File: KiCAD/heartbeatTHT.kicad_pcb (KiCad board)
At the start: 2 copper layers, 48.7 x 39.3 mm, 17 parts, among them Q1 BC547, Q2 BC547, Q3 BC557

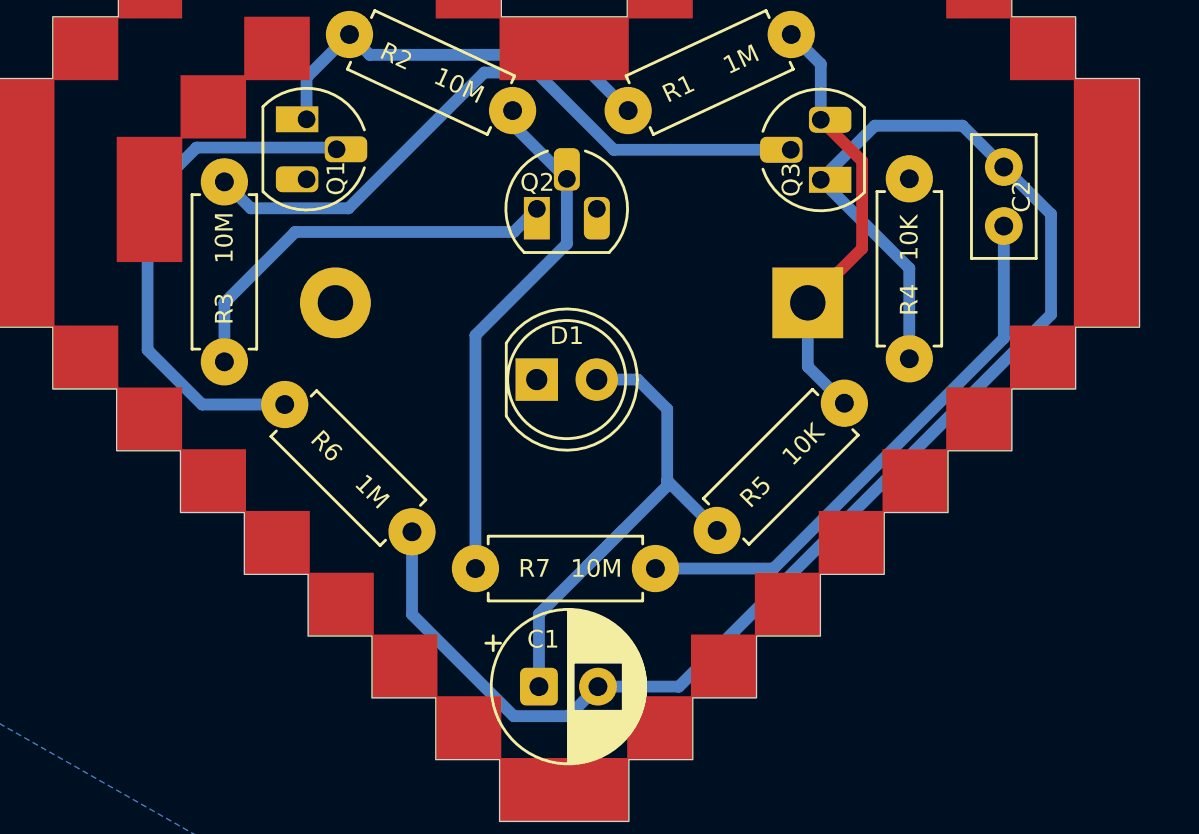
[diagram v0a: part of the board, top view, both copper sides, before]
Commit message: fixed minor issues, added logo, added simulation
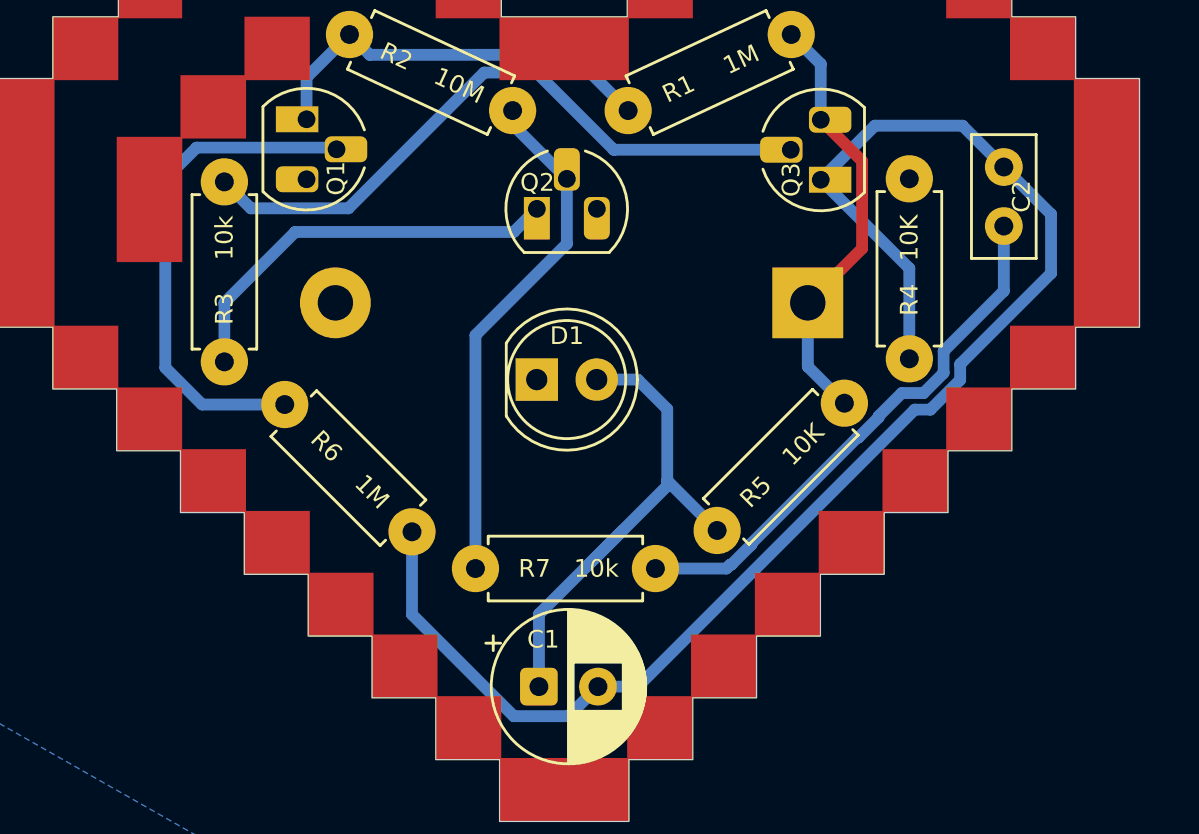
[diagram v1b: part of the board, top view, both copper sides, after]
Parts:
- added blinkyparts_logo_5mm: G***, blinkyparts:logo_5mm, B.Cu at (134.6, 79.4)
- BT1: value Battery_Cell -> 3
- C1: value 100uF -> c=100u
- C2: value 100nF -> 50nF
- R3, R7: value 10M -> 10k
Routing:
- net Net-(Q3-C): track 65.0 -> 64.4 mm
- net Net-(Q1-B): track 22.1 -> 21.5 mm
- net Net-(C2-Pad1): track 23.5 -> 23.0 mm
- added copper zone on B.Cu, net (none)
- removed copper zone on B.Cu, net GND
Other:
- board text added: "CC-BY-NC-SA 4.0"
- board text added: "v1.1"
- board text removed: "v1.0"
